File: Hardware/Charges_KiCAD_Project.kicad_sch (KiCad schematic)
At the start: 25 parts, among them IC1 TP124005-2, J1 796684-4, J2 796684-4, Q1 SI7232DN-T1-GE3, Q2 SI7232DN-T1-GE3

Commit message: updated caps
finished update on cap footprints
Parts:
- C1, C2, C4: footprint Capacitor_THT:CP_Axial_L18.0mm_D6.5mm_P25.00mm_Horizontal -> Capacitor_THT:CP_Axial_L25.0mm_D10.0mm_P30.00mm_Horizontal
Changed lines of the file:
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@@
       (effects (font (size 1.27 1.27)) (justify right))
     )
-    (property "Footprint" "Capacitor_THT:CP_Axial_L18.0mm_D6.5mm_P25.00mm_Horizontal" (id 2) (at 173.99 137.16 0)
+    (property "Footprint" "Capacitor_THT:CP_Axial_L25.0mm_D10.0mm_P30.00mm_Horizontal" (id 2) (at 173.99 137.16 0)
       (effects (font (size 1.27 1.27)) hide)
     )
@@
       (effects (font (size 1.27 1.27)) (justify right))
     )
-    (property "Footprint" "Capacitor_THT:CP_Axial_L18.0mm_D6.5mm_P25.00mm_Horizontal" (id 2) (at 173.99 149.86 0)
+    (property "Footprint" "Capacitor_THT:CP_Axial_L25.0mm_D10.0mm_P30.00mm_Horizontal" (id 2) (at 173.99 149.86 0)
       (effects (font (size 1.27 1.27)) hide)
     )
@@
       (effects (font (size 1.27 1.27)) (justify right))
     )
-    (property "Footprint" "Capacitor_THT:CP_Axial_L18.0mm_D6.5mm_P25.00mm_Horizontal" (id 2) (at 236.22 149.86 0)
+    (property "Footprint" "Capacitor_THT:CP_Axial_L25.0mm_D10.0mm_P30.00mm_Horizontal" (id 2) (at 236.22 149.86 0)
       (effects (font (size 1.27 1.27)) hide)
     )
@@
     )
     (path "/00000000-0000-0000-0000-0000618582e1"
-      (reference "C1") (unit 1) (value "CP1_Small") (footprint "Capacitor_THT:CP_Axial_L18.0mm_D6.5mm_P25.00mm_Horizontal")
+      (reference "C1") (unit 1) (value "CP1_Small") (footprint "Capacitor_THT:CP_Axial_L25.0mm_D10.0mm_P30.00mm_Horizontal")
     )
     (path "/00000000-0000-0000-0000-00006185acbf"
-      (reference "C2") (unit 1) (value "CP1_Small") (footprint "Capacitor_THT:CP_Axial_L18.0mm_D6.5mm_P25.00mm_Horizontal")
+      (reference "C2") (unit 1) (value "CP1_Small") (footprint "Capacitor_THT:CP_Axial_L25.0mm_D10.0mm_P30.00mm_Horizontal")
     )
     (path "/00000000-0000-0000-0000-000061951f00"
@@
     )
     (path "/00000000-0000-0000-0000-000061951ecd"
-      (reference "C4") (unit 1) (value "CP1_Small") (footprint "Capacitor_THT:CP_Axial_L18.0mm_D6.5mm_P25.00mm_Horizontal")
+      (reference "C4") (unit 1) (value "CP1_Small") (footprint "Capacitor_THT:CP_Axial_L25.0mm_D10.0mm_P30.00mm_Horizontal")
     )
     (path "/00000000-0000-0000-0000-000061a437b5/00000000-0000-0000-0000-000061a55586"

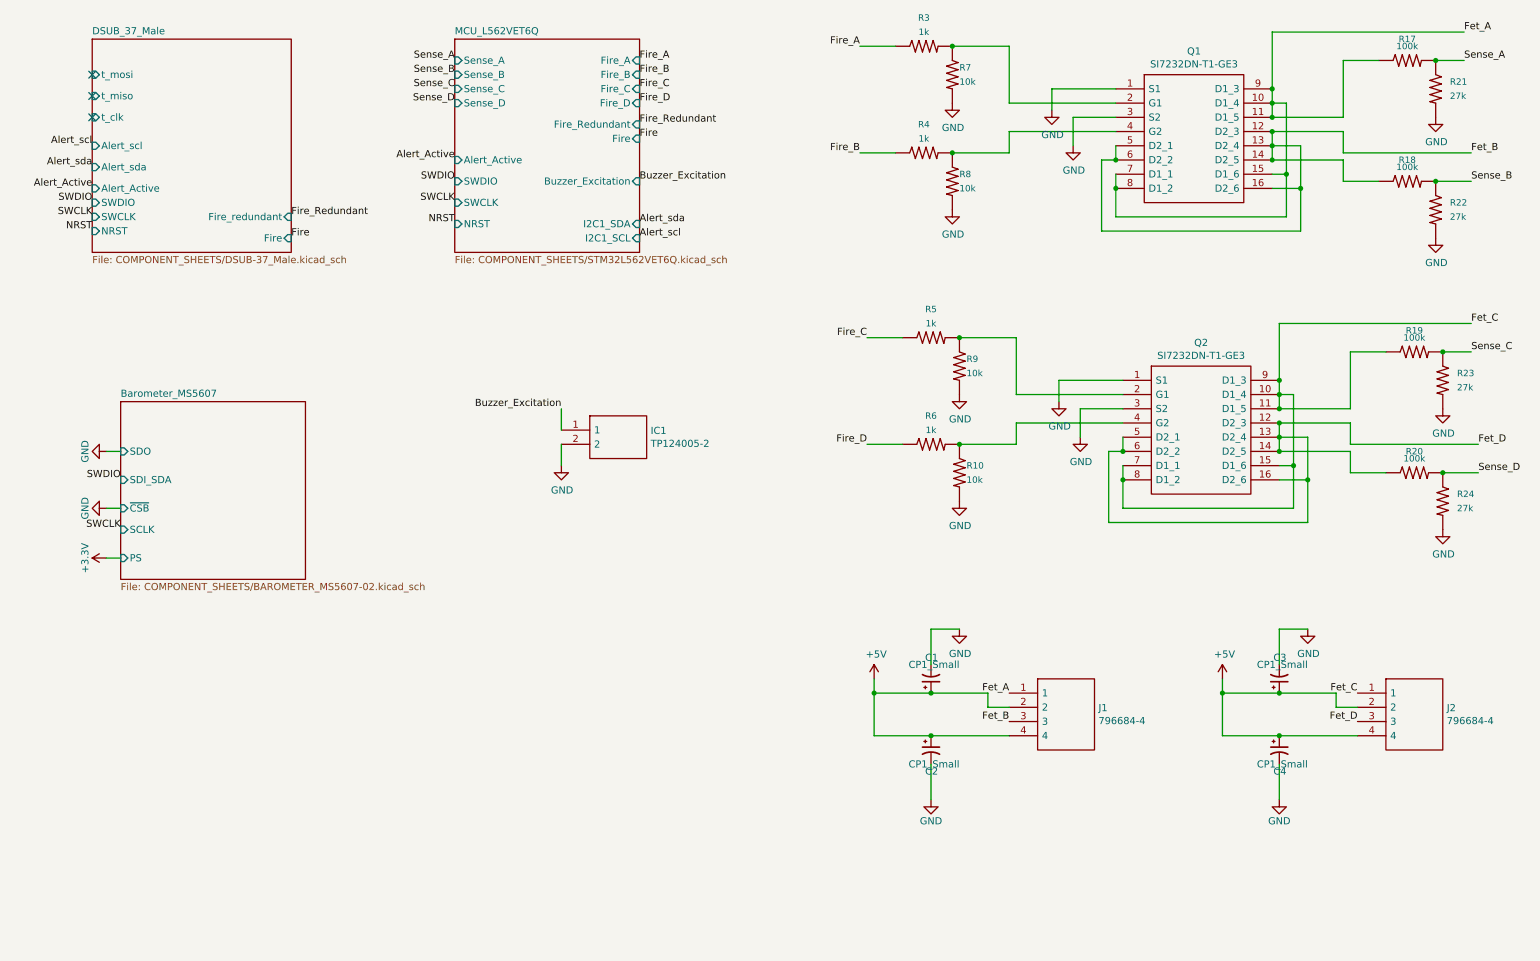
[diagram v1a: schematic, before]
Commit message: Added correct crystal for mcu, re-routing of data lines in progress
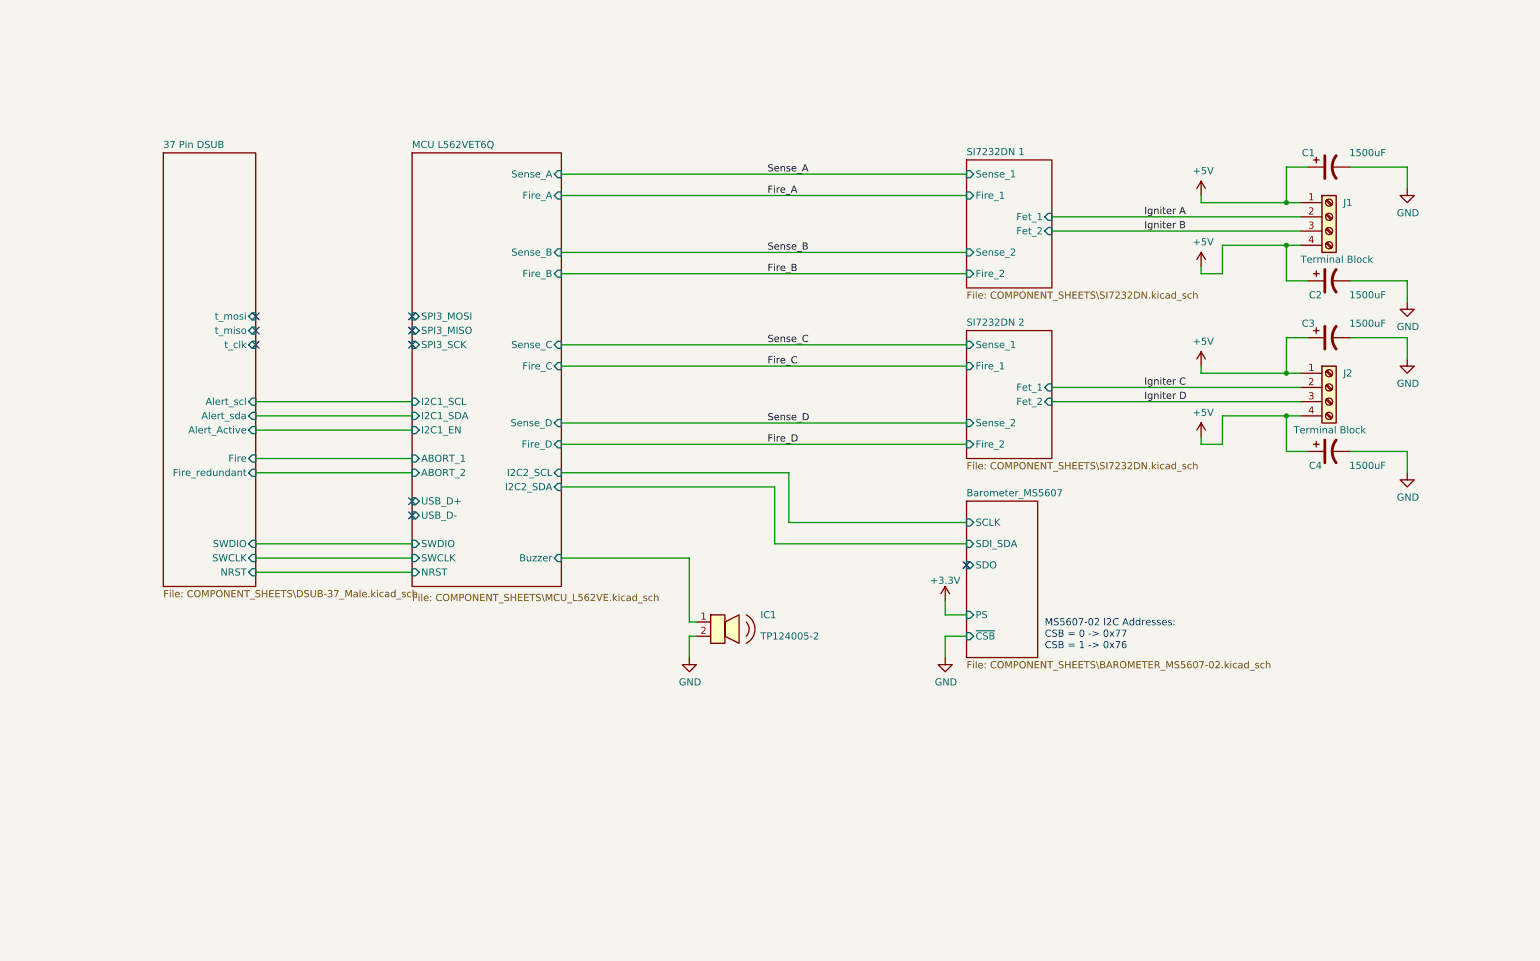
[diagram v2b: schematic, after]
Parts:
- removed C1, C2, C3, C4: CP1_Small, Capacitor_THT:CP_Axial_L25.0mm_D10.0mm_P30.00mm_Horizontal, symbol Device:CP1_Small
- removed IC1: TP124005-2, SamacSys_Parts:TP1240052, symbol Charges_KiCAD_Project-rescue:TP124005-2-SamacSys_Parts
- removed J1, J2: 796684-4, RDT_Custom_Footprints:TB00250004BE, symbol Charges_KiCAD_Project-rescue:TB002-500-04BE-SamacSys_Parts
- removed Q1, Q2: SI7232DN-T1-GE3, SamacSys_Parts:SI7232DNT1GE3, symbol Charges_KiCAD_Project-rescue:SI7232DN-T1-GE3-SamacSys_Parts
- removed R10, R7, R8, R9: 10k, Resistor_SMD:R_0603_1608Metric_Pad1.05x0.95mm_HandSolder, symbol Charges_KiCAD_Project-rescue:RESISTOR0402-SparkFun-Resistors
- removed R17, R18, R19, R20: 100k, Resistor_SMD:R_0603_1608Metric_Pad1.05x0.95mm_HandSolder, symbol Charges_KiCAD_Project-rescue:RESISTOR0402-SparkFun-Resistors
- removed R21, R22, R23, R24: 27k, Resistor_SMD:R_0603_1608Metric_Pad1.05x0.95mm_HandSolder, symbol Charges_KiCAD_Project-rescue:RESISTOR0402-SparkFun-Resistors
- removed R3, R4, R5, R6: 1k, Resistor_SMD:R_0603_1608Metric_Pad1.05x0.95mm_HandSolder, symbol Charges_KiCAD_Project-rescue:RESISTOR0402-SparkFun-Resistors
- added C1, C2, C3, C4: 1500uF, Capacitor_THT:CP_Axial_L18.0mm_D6.5mm_P25.00mm_Horizontal, symbol Device:C_Polarized_US
- added IC1: TP124005-2, Buzzer_Beeper:Buzzer_TDK_PS1240P02BT_D12.2mm_H6.5mm, symbol dk_Alarms-Buzzers-and-Sirens:PKMCS0909E4000-R1
- added J1, J2: Terminal Block, RDT_Custom_Footprints:TB00250004BE, symbol Connector:Screw_Terminal_01x04
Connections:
- net +5V: now also C1.1, C2.1, C3.1, C4.1, J1.1 (Pin_1), J1.4 (Pin_4), J2.1 (Pin_1), J2.4 (Pin_4)
- net GND: now also C1.2, C2.2, C3.2, C4.2, IC1.2
- new net Igniter A: J1.2 (Pin_2)
- new net Igniter B: J1.3 (Pin_3)
- new net Igniter C: J2.2 (Pin_2)
- new net Igniter D: J2.3 (Pin_3)
- new net MCU L562VET6Q/Buzzer: IC1.1
- no-connect marks 3 -> 9
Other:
- removed sheet DSUB_37_Male
- removed sheet MCU_L562VET6Q
- added sheet 37 Pin DSUB (COMPONENT_SHEETS\DSUB-37_Male.kicad_sch)
- added sheet MCU L562VET6Q (COMPONENT_SHEETS\MCU_L562VE.kicad_sch)
- added sheet SI7232DN 1 (COMPONENT_SHEETS\SI7232DN.kicad_sch)
- added sheet SI7232DN 2 (COMPONENT_SHEETS\SI7232DN.kicad_sch)
- sheet Barometer_MS5607: file COMPONENT_SHEETS/BAROMETER_MS5607-02.kicad_sch -> COMPONENT_SHEETS\BAROMETER_MS5607-02.kicad_sch
- note added: "MS5607-02 I2C Addresses: CSB = 0 -> 0x77 CSB = 1 -> 0x76"

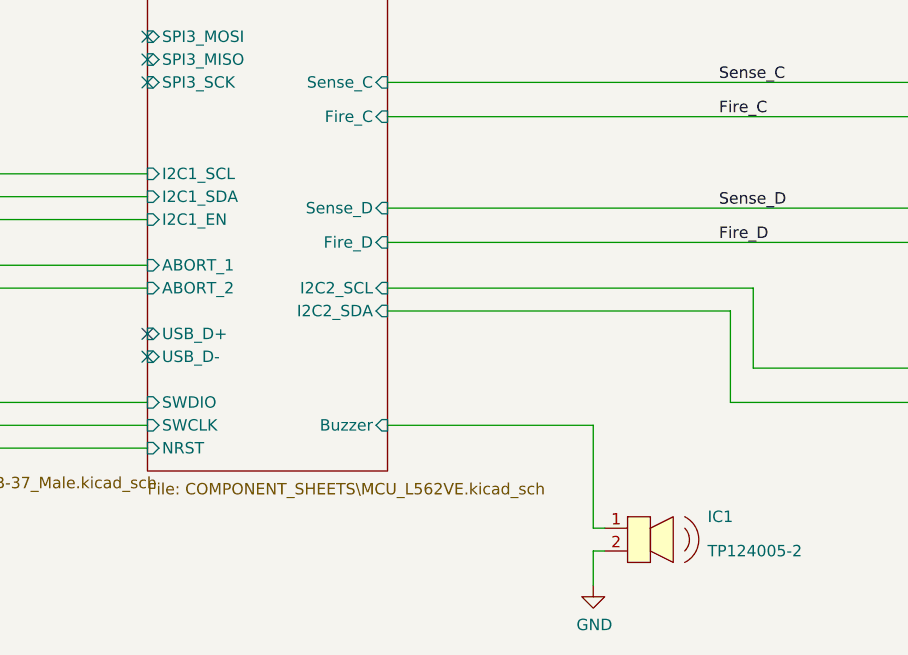
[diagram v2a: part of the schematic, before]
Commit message: Routed Alert I2C lines
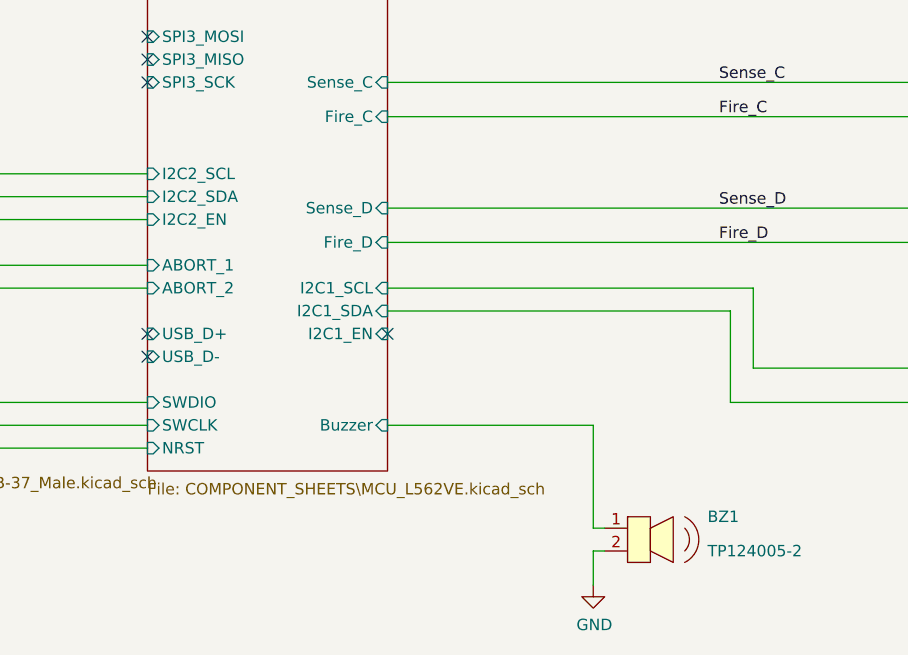
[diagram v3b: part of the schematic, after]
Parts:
- renumbered IC1 to BZ1
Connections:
- no-connect marks 9 -> 10
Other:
- sheet MCU L562VET6Q ports: added I2C2_EN; removed none
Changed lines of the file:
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@@
   (no_connect (at 81.28 77.47))
   (no_connect (at 81.28 74.93))
+  (no_connect (at 107.95 105.41))
   (no_connect (at 81.28 105.41))
   (no_connect (at 81.28 72.39))
@@
   (symbol (lib_id "dk_Alarms-Buzzers-and-Sirens:PKMCS0909E4000-R1") (at 134.62 129.54 0) (unit 1)
     (in_bom yes) (on_board yes)
-    (property "Reference" "IC1" (id 0) (at 143.51 125.73 0)
+    (property "Reference" "BZ1" (id 0) (at 143.51 125.73 0)
       (effects (font (size 1.27 1.27)) (justify left))
     )
@@
       (effects (font (size 1.27 1.27)) (justify left top))
     )
-    (pin "I2C1_EN" input (at 81.28 92.71 180)
-      (effects (font (size 1.27 1.27)) (justify left))
+    (pin "I2C1_EN" input (at 107.95 105.41 0)
+      (effects (font (size 1.27 1.27)) (justify right))
     )
     (pin "USB_D+" input (at 81.28 105.41 180)
@@
       (effects (font (size 1.27 1.27)) (justify left))
     )
-    (pin "I2C1_SCL" input (at 81.28 87.63 180)
-      (effects (font (size 1.27 1.27)) (justify left))
-    )
-    (pin "I2C1_SDA" input (at 81.28 90.17 180)
-      (effects (font (size 1.27 1.27)) (justify left))
+    (pin "I2C1_SCL" input (at 107.95 100.33 0)
+      (effects (font (size 1.27 1.27)) (justify right))
+    )
+    (pin "I2C1_SDA" input (at 107.95 102.87 0)
+      (effects (font (size 1.27 1.27)) (justify right))
     )
     (pin "Fire_C" input (at 107.95 81.28 0)
@@
       (effects (font (size 1.27 1.27)) (justify right))
     )
-    (pin "I2C2_SCL" input (at 107.95 100.33 0)
-      (effects (font (size 1.27 1.27)) (justify right))
-    )
-    (pin "I2C2_SDA" input (at 107.95 102.87 0)
-      (effects (font (size 1.27 1.27)) (justify right))
+    (pin "I2C2_SCL" input (at 81.28 87.63 180)
+      (effects (font (size 1.27 1.27)) (justify left))
+    )
+    (pin "I2C2_SDA" input (at 81.28 90.17 180)
+      (effects (font (size 1.27 1.27)) (justify left))
+    )
+    (pin "I2C2_EN" input (at 81.28 92.71 180)
+      (effects (font (size 1.27 1.27)) (justify left))
     )
   )
@@
       (reference "#PWR049") (unit 1) (value "+3.3V") (footprint "")
     )
+    (path "/2af26db1-9ad4-40ce-8fd2-07c86680a0ae"
+      (reference "BZ1") (unit 1) (value "TP124005-2") (footprint "Buzzer_Beeper:Buzzer_TDK_PS1240P02BT_D12.2mm_H6.5mm")
+    )
     (path "/3c130d64-9137-4c65-8366-1112524f50cc"
       (reference "C1") (unit 1) (value "1500uF") (footprint "Capacitor_THT:CP_Axial_L18.0mm_D6.5mm_P25.00mm_Horizontal")
@@
       (reference "D5") (unit 1) (value "Red") (footprint "LED_SMD:LED_0603_1608Metric_Pad1.05x0.95mm_HandSolder")
     )
-    (path "/2af26db1-9ad4-40ce-8fd2-07c86680a0ae"
-      (reference "IC1") (unit 1) (value "TP124005-2") (footprint "Buzzer_Beeper:Buzzer_TDK_PS1240P02BT_D12.2mm_H6.5mm")
-    )
     (path "/201b9629-4d06-4d75-891f-9f18d99b784e"

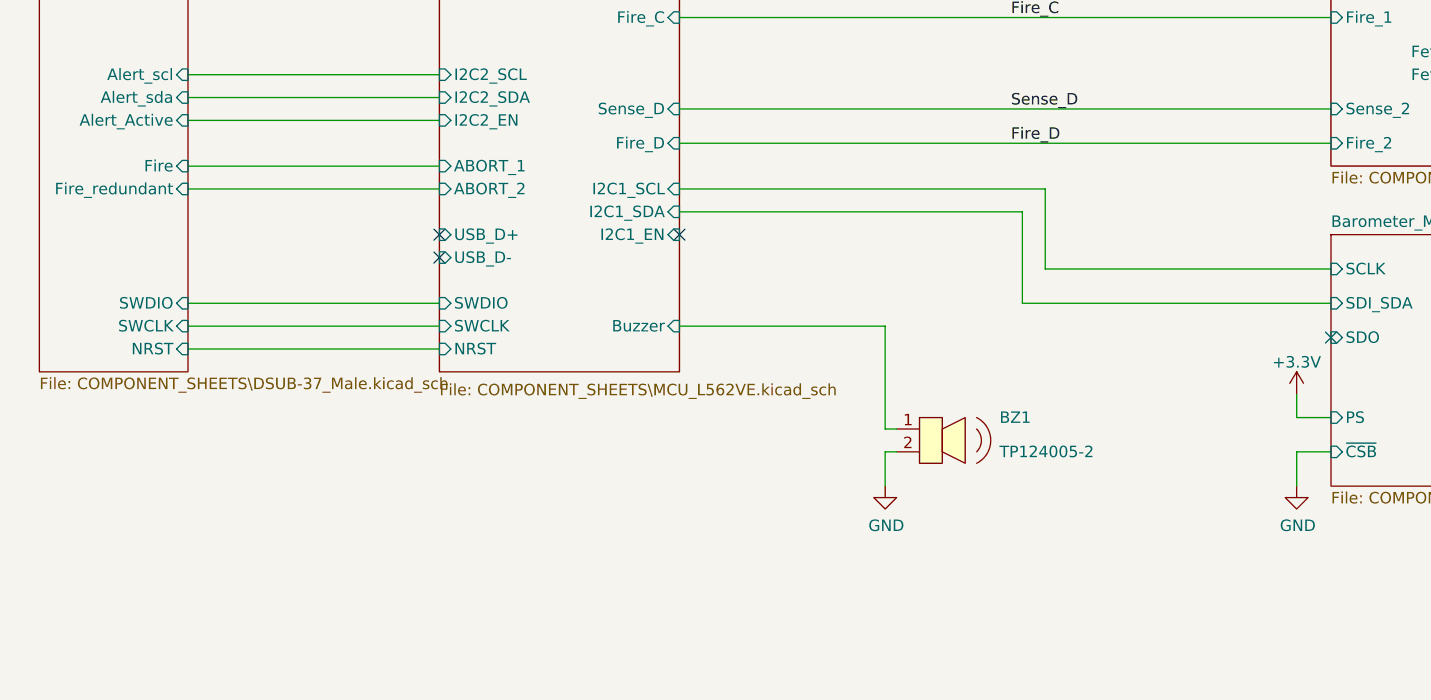
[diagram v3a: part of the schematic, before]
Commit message: Routed all traces and components, need to place LEDs
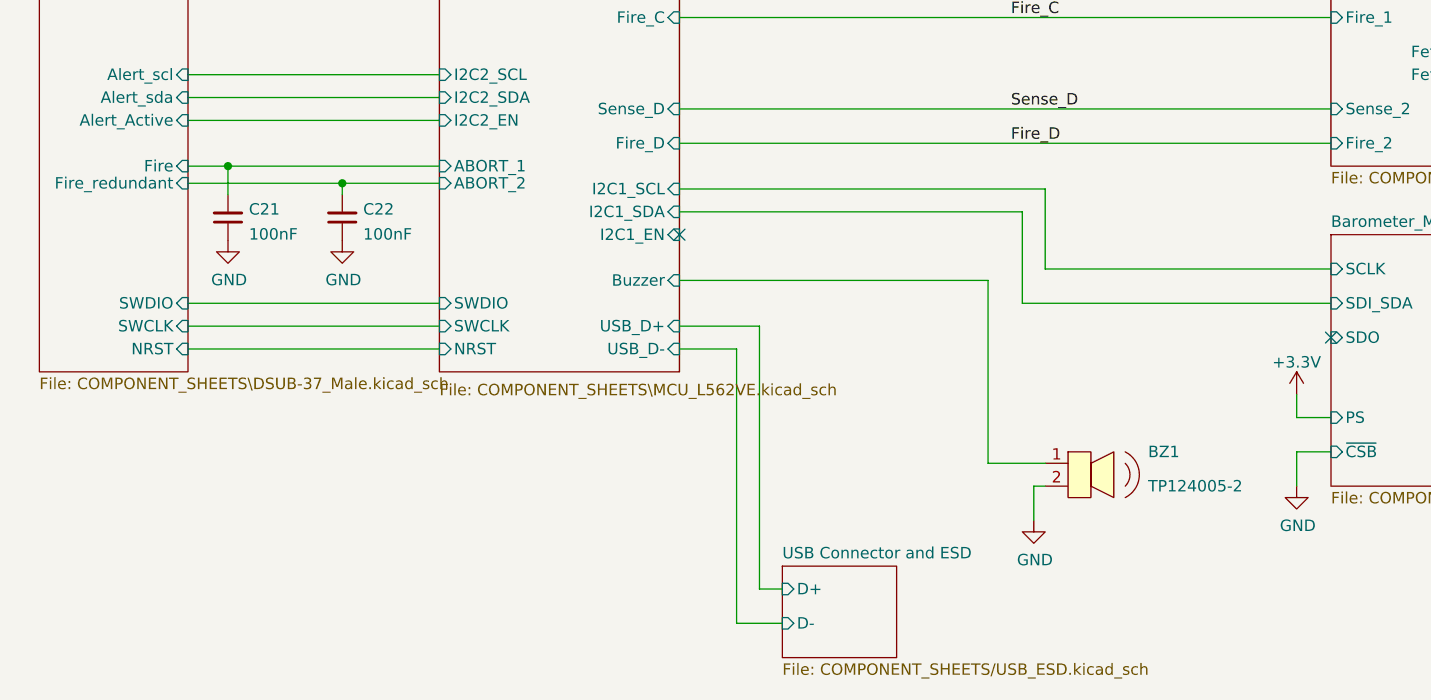
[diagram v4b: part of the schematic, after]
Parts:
- added C21, C22: 100nF, Capacitor_SMD:C_0603_1608Metric_Pad1.08x0.95mm_HandSolder, symbol Device:C_Small
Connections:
- net 37 Pin DSUB/Fire: now also C21.2
- net 37 Pin DSUB/Fire_redundant: now also C22.2
- net GND: now also C21.1, C22.1
- no-connect marks 10 -> 8
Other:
- added sheet USB Connector and ESD (COMPONENT_SHEETS/USB_ESD.kicad_sch)
- moved on the sheet: BZ1
